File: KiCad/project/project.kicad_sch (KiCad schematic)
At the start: 25 parts, among them P1 TerminalBlock 5P 5.0mm, U1 DRV8313PWPR

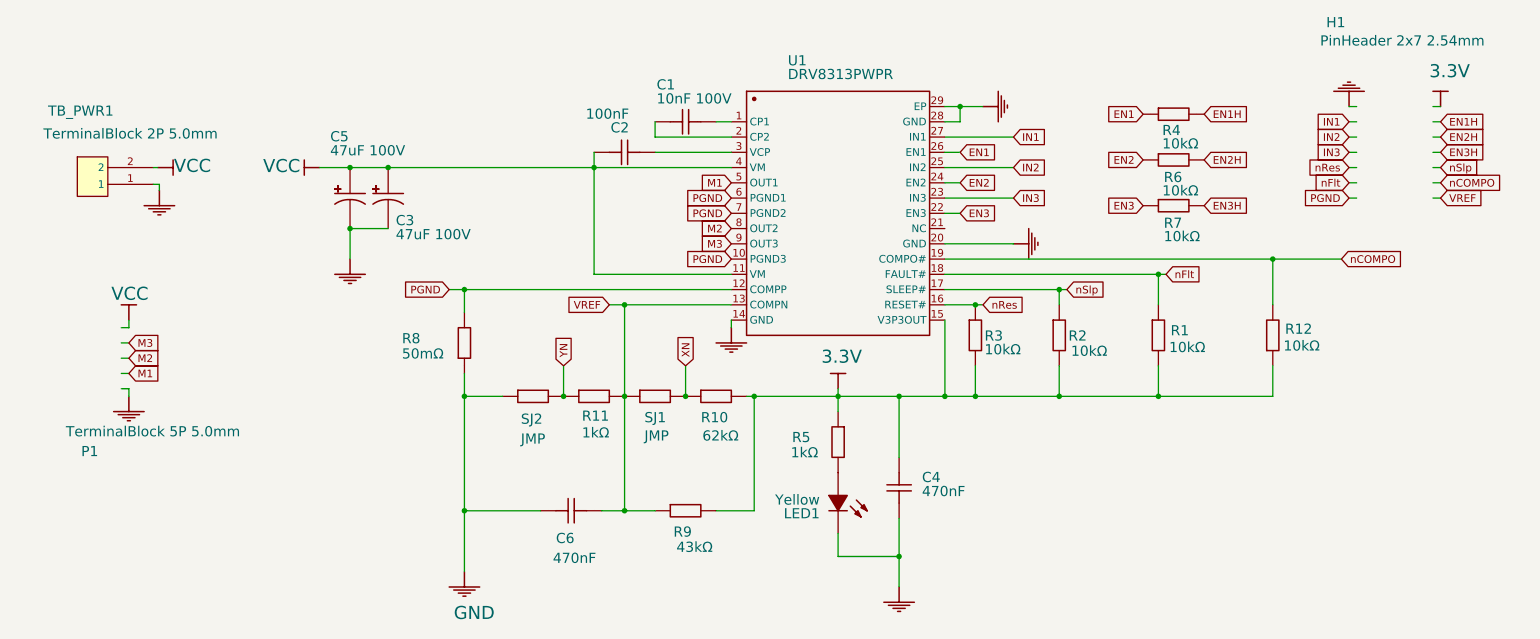
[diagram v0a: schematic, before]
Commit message: Add VM decoupling caps (C7/C8); delete planning docs; reconcile docs
Datasheet conformance: the DRV8313 VM pin spec calls for two 0.1 uF
VM->GND ceramics (one per VM pin) in addition to the bulk cap; the board
had bulk only. Added C7/C8 = 100nF/100V 0603 (Samsung CL10B104KC8NNNC /
LCSC C15725), each wired VCC(VM)<->GND (netlist-verified one pin per net).
PCB placement at U1 pins 4 & 11 + routing still pending.

Docs: deleted the now-complete redesign-plan.html / redesign-bom.md
planning docs and fixed the references/inconsistencies they left behind:
- README: docs/ row trimmed to datasheets; status now "DRC-clean (0 errors)"
  with ERC items called out as EasyEDA-import artifacts (not real errors).
- CLAUDE.md: Goal & status (redesign complete), Repository layout (dropped
  the removed Altium/EasyEDA/Gerber/3D/PnP dirs), as-built Components list,
  cleared dangling redesign-bom refs.
- ERC baseline reconciled 141 -> 101 (check_design.py, tools/README.md,
  CLAUDE.md): 141 pre-redo, 91 post-redo, 101 with C7/C8 added.

All hard checks pass: DRC 0 error-severity, all nets connected, 0
clearance/shorts; ERC 101 = baseline (import artifacts only, 0 new errors).

Co-Authored-By: Claude Opus 4.8 (1M context) <noreply@anthropic.com>
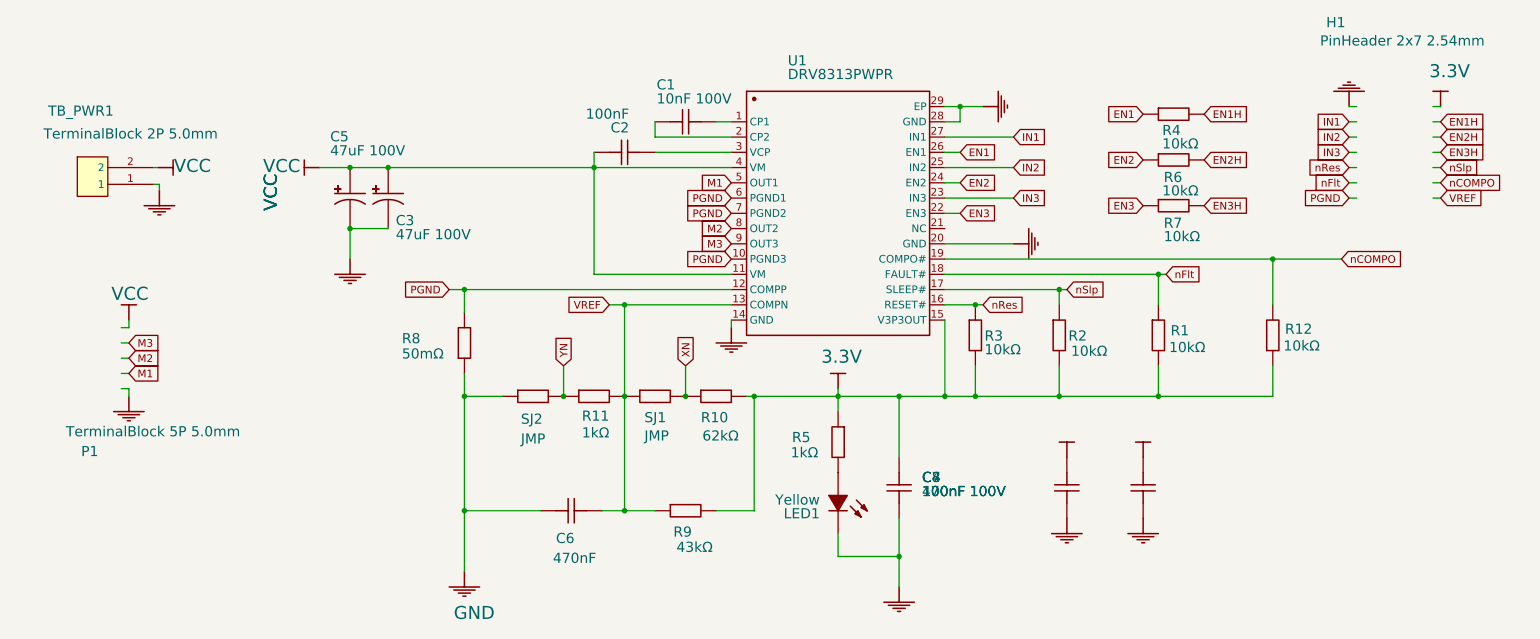
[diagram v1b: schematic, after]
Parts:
- added C7, C8: 100nF 100V, simplefocmini:C0603, symbol CC0603ZRY5V6BB474
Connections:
- net GND: now also C7.1, C8.1
- net VCC: now also C7.2, C8.2
